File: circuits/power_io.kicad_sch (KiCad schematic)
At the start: 37 parts, among them J5 LASER PSU, J6 EXT 5V, U11 AP2112K-3.3, U12 INA4180A1, U13 LM4040C50 5V, U14 AD7606BSTZ-4

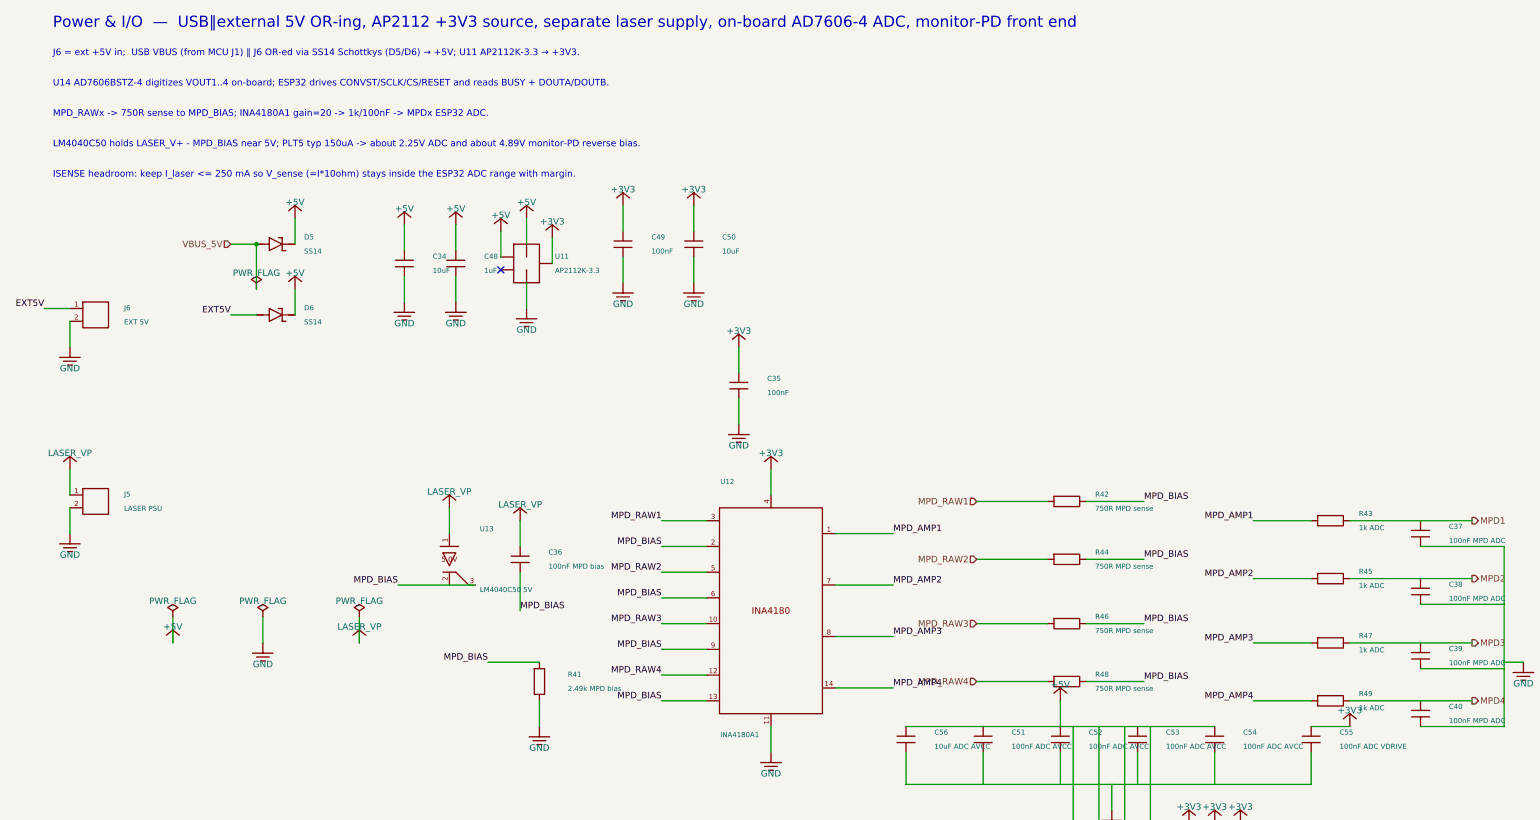
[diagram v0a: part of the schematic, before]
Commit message: add onboard laser controller supplies
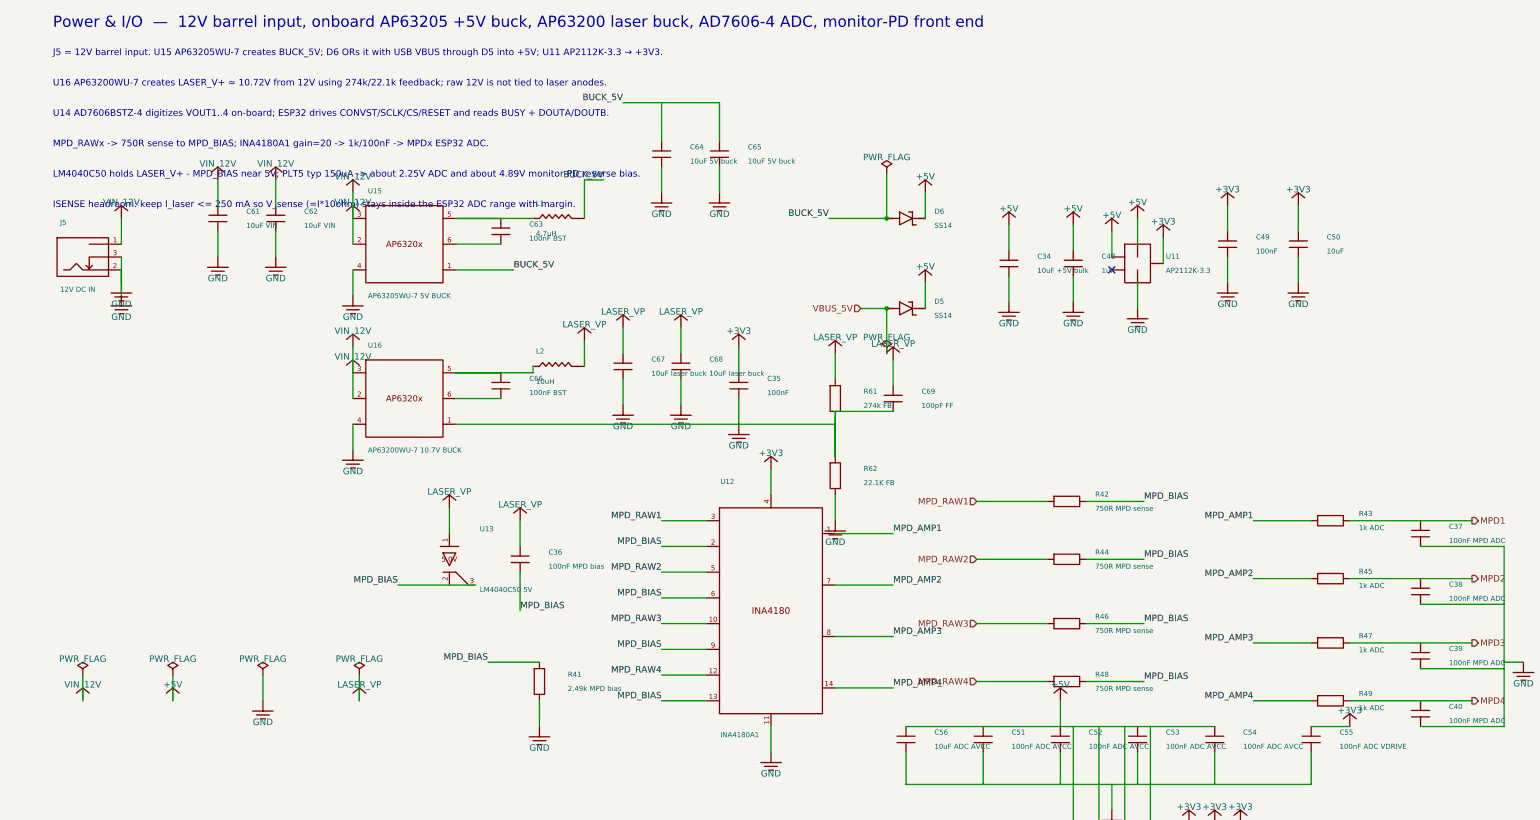
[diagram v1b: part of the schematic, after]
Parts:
- removed J5: LASER PSU, Connector_PinHeader_2.54mm:PinHeader_1x02_P2.54mm_Vertical, symbol viv:CONN2
- removed J6: EXT 5V, Connector_PinHeader_2.54mm:PinHeader_1x02_P2.54mm_Vertical, symbol viv:CONN2
- added C61, C62: 10uF VIN, Capacitor_SMD:C_0805_2012Metric_Pad1.18x1.45mm_HandSolder, symbol viv:C_V
- added C63, C66: 100nF BST, Capacitor_SMD:C_0402_1005Metric_Pad0.74x0.62mm_HandSolder, symbol viv:C_V
- added C64, C65: 10uF 5V buck, Capacitor_SMD:C_0805_2012Metric_Pad1.18x1.45mm_HandSolder, symbol viv:C_V
- added C67, C68: 10uF laser buck, Capacitor_SMD:C_0805_2012Metric_Pad1.18x1.45mm_HandSolder, symbol viv:C_V
- added C69: 100pF FF, Capacitor_SMD:C_0402_1005Metric_Pad0.74x0.62mm_HandSolder, symbol viv:C_V
- added D5: SS14, Diode_SMD:D_SMA, symbol viv:SCHOTTKY
- added L1: 4.7uH, Open_Automation:L_5.4x5.3_H3, symbol viv:L_H
- added L2: 10uH, Open_Automation:L_4x4, symbol viv:L_H
- added R61: 274k FB, Resistor_SMD:R_0603_1608Metric_Pad0.98x0.95mm_HandSolder, symbol viv:R_V
- added R62: 22.1K FB, Resistor_SMD:R_0402_1005Metric_Pad0.72x0.64mm_HandSolder, symbol viv:R_V
- added U15: AP63205WU-7 5V BUCK, Package_TO_SOT_SMD:TSOT-23-6, symbol viv:AP6320X_TSOT6
- added U16: AP63200WU-7 10.7V BUCK, Package_TO_SOT_SMD:TSOT-23-6, symbol viv:AP6320X_TSOT6
- C34: value 10uF -> 10uF +5V bulk
- J5: renamed from D5; value SS14 -> 12V DC IN; footprint Diode_SMD:D_SMA -> Open_Automation:BarrelJack_OD5.5_ID2.5; symbol viv:SCHOTTKY -> viv:BARREL_JACK_SWITCH; LCSC C2480 -> C194407; Part Number SS14 -> DC-470-2.1GP
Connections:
- net +5V: now also D5.2 (K); no longer J5.2 (K)
- net GND: now also J5.2, J5.3, C61.2, C62.2, C64.2, C65.2, C67.2, C68.2, R62.2, U15.4 (GND), U16.4 (GND)
- net LASER_V+: now also C67.1, C68.1, C69.1, L2.2, R61.1
- net VBUS_5V: now also D5.1 (A); no longer J5.1 (A)
- net EXT5V renamed BUCK_5V
- net BUCK_5V: now also C64.1, C65.1, L1.2, U15.1 (FB)
- new net: C63.1, L1.1, U15.5 (SW)
- new net: C63.2, U15.6 (BST)
- new net: C69.2, R61.2, R62.1, U16.1 (FB)
- new net: C66.1, L2.1, U16.5 (SW)
- new net: C66.2, U16.6 (BST)
- new net VIN_12V: C61.1, C62.1, J5.1, U15.2 (EN), U15.3 (IN), U16.2 (EN), U16.3 (IN)
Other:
- note added: "J5 = 12V barrel input. U15 AP63205WU-7 creates BUCK_5V; D6 ORs it with USB VBUS through D5 into +5V; U11 AP2112K-3.3 → +3V3."
- note added: "Power & I/O — 12V barrel input, onboard AP63205 +5V buck, AP63200 laser buck, AD7606-4 ADC, monitor-PD front end"
- note added: "U16 AP63200WU-7 creates LASER_V+ ≈ 10.72V from 12V using 274k/22.1k feedback; raw 12V is not tied to laser anodes."
- note removed: "J6 = ext +5V in; USB VBUS (from MCU J1) ‖ J6 OR-ed via SS14 Schottkys (D5/D6) → +5V; U11 AP2112K-3.3 → +3V3."
- note removed: "Power & I/O — USB‖external 5V OR-ing, AP2112 +3V3 source, separate laser supply, on-board AD7606-4 ADC, monitor-PD front end"

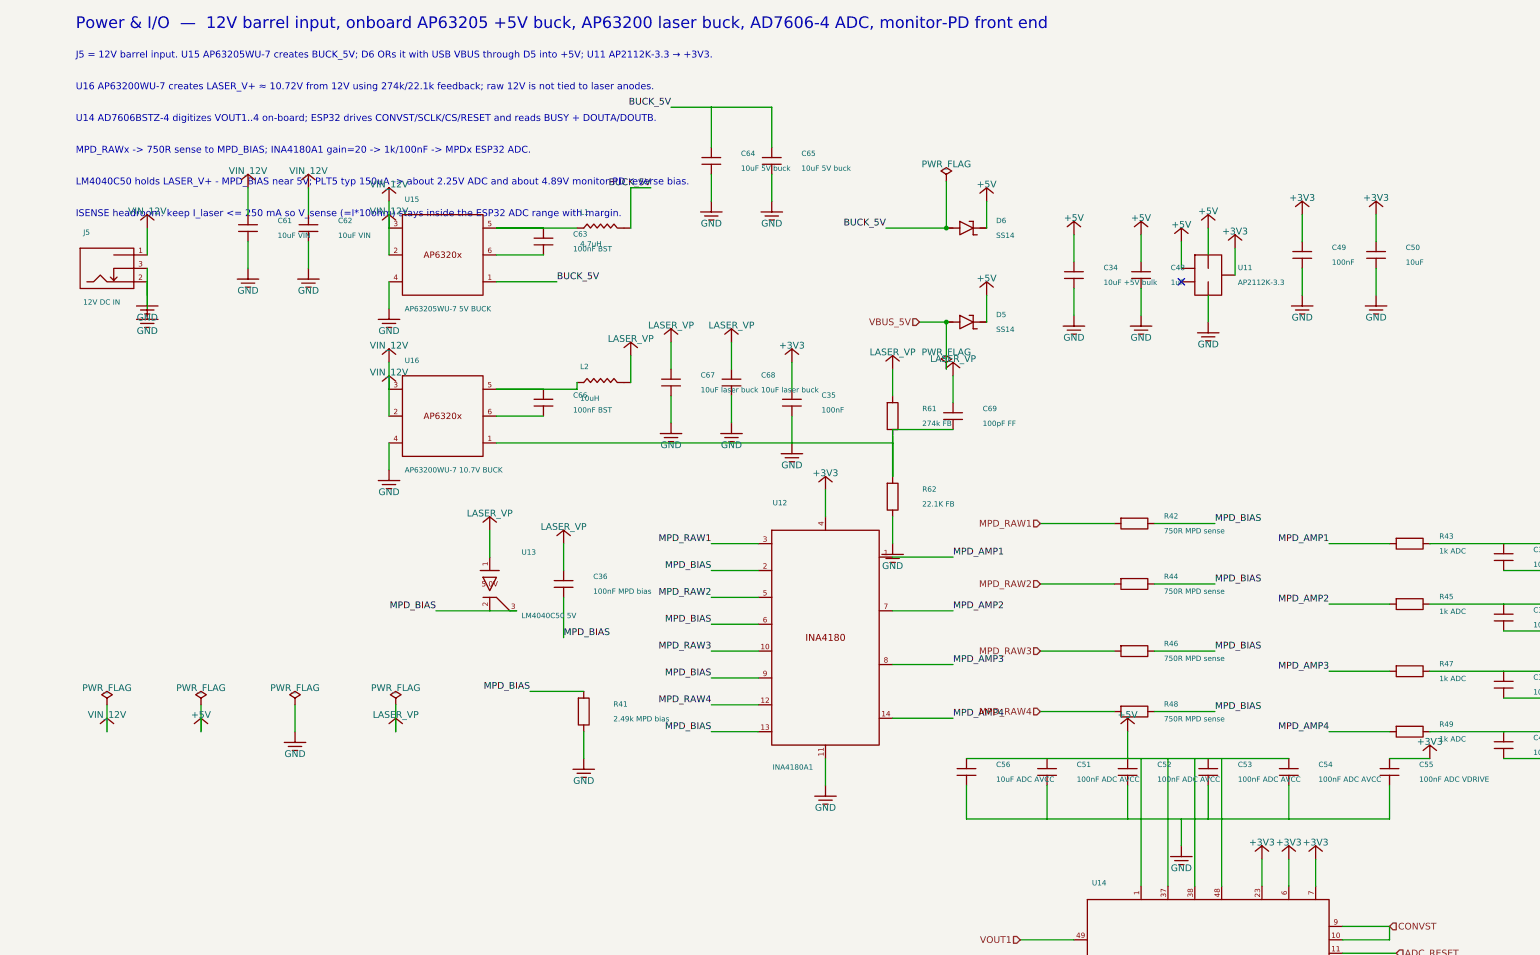
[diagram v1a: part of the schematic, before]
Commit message: Regenerate 24V power IO schematic
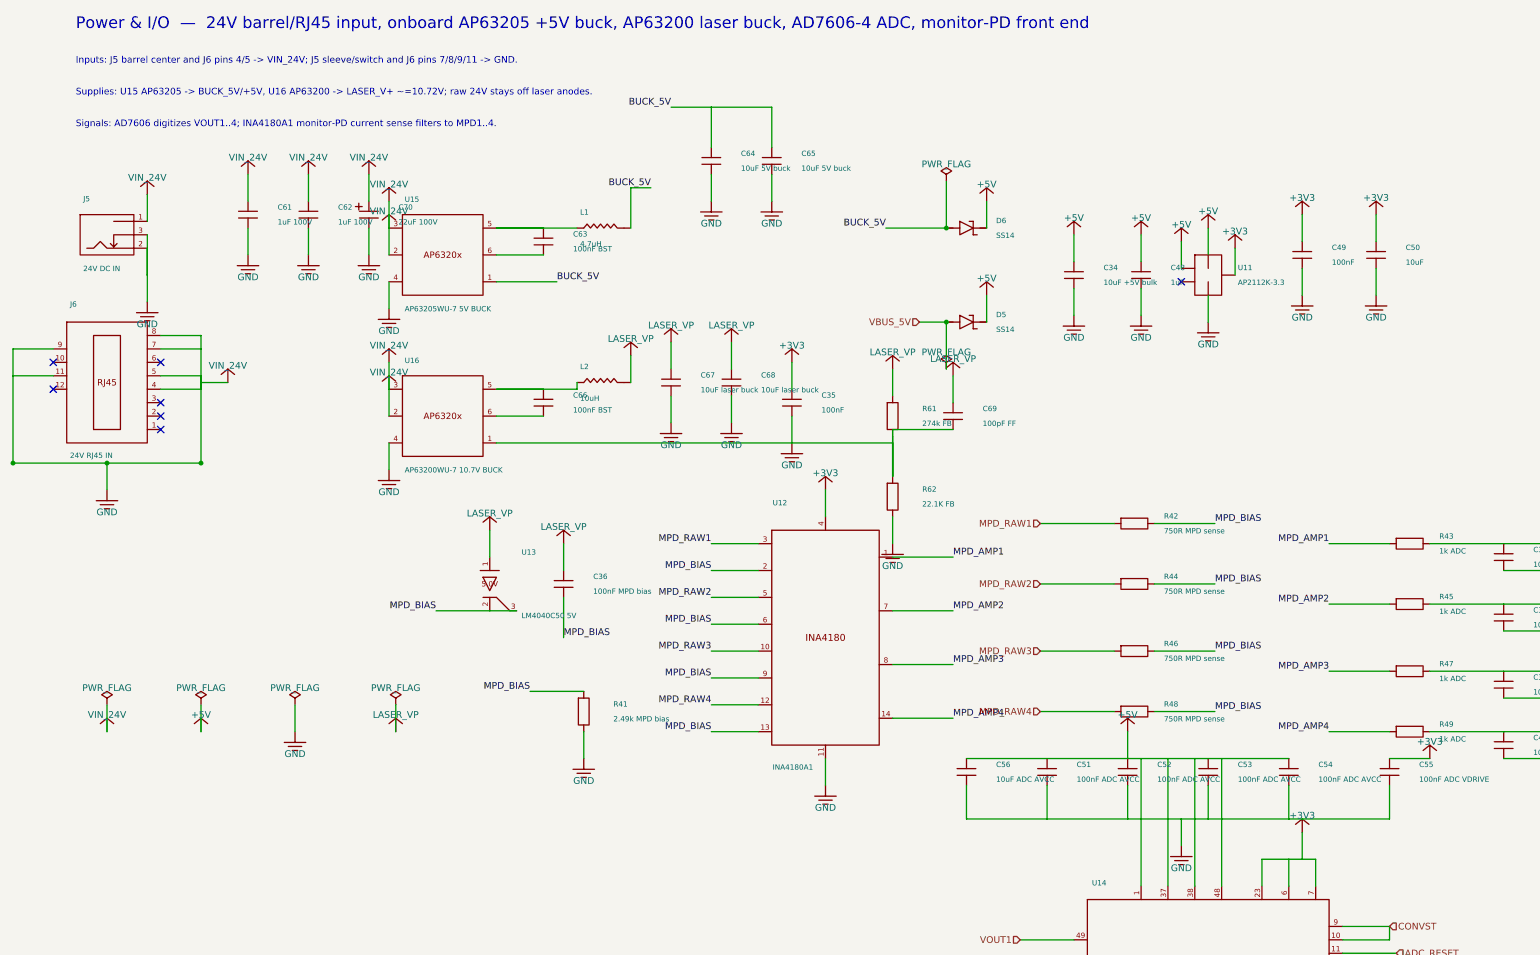
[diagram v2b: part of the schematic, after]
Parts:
- removed C48: 1uF, Capacitor_SMD:C_0402_1005Metric_Pad0.74x0.62mm_HandSolder, symbol viv:C_V
- removed C49: 100nF, Capacitor_SMD:C_0402_1005Metric_Pad0.74x0.62mm_HandSolder, symbol viv:C_V
- removed C50: 10uF, Capacitor_SMD:C_0805_2012Metric_Pad1.18x1.45mm_HandSolder, symbol viv:C_V
- removed C62: 10uF VIN, Capacitor_SMD:C_0805_2012Metric_Pad1.18x1.45mm_HandSolder, symbol viv:C_V
- removed U13: LM4040C50 5V, Package_TO_SOT_SMD:SOT-23, symbol viv:LM4040_DBZ
- removed U15: AP63205WU-7 5V BUCK, Package_TO_SOT_SMD:TSOT-23-6, symbol viv:AP6320X_TSOT6
- removed U16: AP63200WU-7 10.7V BUCK, Package_TO_SOT_SMD:TSOT-23-6, symbol viv:AP6320X_TSOT6
- added C63, C66: 100nF BST, Capacitor_SMD:C_0402_1005Metric_Pad0.74x0.62mm_HandSolder, symbol viv:C_V
- added C64, C65: 10uF 5V buck, Capacitor_SMD:C_0805_2012Metric_Pad1.18x1.45mm_HandSolder, symbol viv:C_V
- added C67, C68: 10uF laser buck, Capacitor_SMD:C_0805_2012Metric_Pad1.18x1.45mm_HandSolder, symbol viv:C_V
- added L1: 4.7uH, Open_Automation:L_5.4x5.3_H3, symbol viv:L_H
- added L2: 10uH, Open_Automation:L_4x4, symbol viv:L_H
- added R43: 1k ADC, Resistor_SMD:R_0603_1608Metric_Pad0.98x0.95mm_HandSolder, symbol viv:R_H
- C48: renamed from L2; value 10uH -> 1uF; footprint Open_Automation:L_4x4 -> Capacitor_SMD:C_0402_1005Metric_Pad0.74x0.62mm_HandSolder; symbol viv:L_H -> viv:C_V; LCSC C98364 -> C7472946; Part Number WPN4020H100MT -> HGC0402R5105K250NTEJ
- C49: renamed from C66; value 100nF BST -> 100nF
- C50: renamed from C67; value 10uF laser buck -> 10uF
- C61: renamed from L1; value 4.7uH -> 1uF 100V; footprint Open_Automation:L_5.4x5.3_H3 -> Capacitor_SMD:C_1206_3216Metric_Pad1.33x1.80mm_HandSolder; symbol viv:L_H -> viv:C_V; LCSC C408410 -> C13832; Part Number MWSA0503S-4R7MT -> CL31B105KCHNNNE
- C62: renamed from C63; value 100nF BST -> 1uF 100V; footprint Capacitor_SMD:C_0402_1005Metric_Pad0.74x0.62mm_HandSolder -> Capacitor_SMD:C_1206_3216Metric_Pad1.33x1.80mm_HandSolder; LCSC C83056 -> C13832; Part Number 0402B104K160CT -> CL31B105KCHNNNE
- C70: renamed from C64; value 10uF 5V buck -> 22uF 100V; footprint Capacitor_SMD:C_0805_2012Metric_Pad1.18x1.45mm_HandSolder -> Capacitor_SMD:C_Elec_8x10.2; symbol viv:C_V -> viv:C_POL_V; LCSC C318691 -> C90264; Part Number CL21A106KAYNNNG -> RVT2A220M0810
- J5: value 12V DC IN -> 24V DC IN
- J6: renamed from C61; value 10uF VIN -> 24V RJ45 IN; footprint Capacitor_SMD:C_0805_2012Metric_Pad1.18x1.45mm_HandSolder -> Connector_RJ:RJ45_Amphenol_RJHSE538X; symbol viv:C_V -> viv:CONN_RJ45; LCSC C318691 -> C386757; Part Number CL21A106KAYNNNG -> R-RJ45R08P-C000
- U13: renamed from R43; value 1k ADC -> LM4040C50 5V; footprint Resistor_SMD:R_0603_1608Metric_Pad0.98x0.95mm_HandSolder -> Package_TO_SOT_SMD:SOT-23; symbol viv:R_H -> viv:LM4040_DBZ; LCSC C2907002 -> C69316; Part Number FRC0603F1001TS -> LM4040C50IDBZR
- U15: renamed from C65; value 10uF 5V buck -> AP63205WU-7 5V BUCK; footprint Capacitor_SMD:C_0805_2012Metric_Pad1.18x1.45mm_HandSolder -> Package_TO_SOT_SMD:TSOT-23-6; symbol viv:C_V -> viv:AP6320X_TSOT6; LCSC C318691 -> C2071056; Part Number CL21A106KAYNNNG -> AP63205WU-7
- U16: renamed from C68; value 10uF laser buck -> AP63200WU-7 10.7V BUCK; footprint Capacitor_SMD:C_0805_2012Metric_Pad1.18x1.45mm_HandSolder -> Package_TO_SOT_SMD:TSOT-23-6; symbol viv:C_V -> viv:AP6320X_TSOT6; LCSC C318691 -> C2071868; Part Number CL21A106KAYNNNG -> AP63200WU-7
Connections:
- net +3V3: now also C49.1, C50.1
- net +5V: now also C48.1
- net BUCK_5V: now also C64.1, C65.1, L1.2; no longer C61.2, C70.1
- net GND: now also C48.2, C49.2, C61.1, C61.2, C62.1, C62.2, C70.1 (+), J5.1, J6.11, J6.4, J6.5, J6.7, J6.8, J6.9, U15.3 (IN), U15.4 (GND), U16.3 (IN), U16.4 (GND), C64.2, C65.2, C67.2, C68.2; no longer J6.2
- net LASER_V+: now also U13.1 (K), C67.1, C68.1, L2.2; no longer C48.2, C50.1, U16.1
- net MPD1: now also R43.2; no longer U13.2
- net MPD_AMP1: now also R43.1; no longer U13.1
- net MPD_BIAS: now also U13.2 (A), U13.3 (*)
- net at C69.2, R61.2, R62.1: now also U16.1 (FB)
- net VIN_12V: no longer names the net of J6.1
- net VIN_12V: no longer J5.1
- new net: C63.1, L1.1, U15.5 (SW)
- new net: C63.2, U15.6 (BST)
- new net: C66.1, L2.1, U16.5 (SW)
- new net: C66.2, U16.6 (BST)
- no-connect marks 2 -> 8
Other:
- note added: "Inputs: J5 barrel center and J6 pins 4/5 -> VIN_24V; J5 sleeve/switch and J6 pins 7/8/9/11 -> GND."
- note added: "Power & I/O — 24V barrel/RJ45 input, onboard AP63205 +5V buck, AP63200 laser buck, AD7606-4 ADC, monitor-PD front end"
- note added: "Signals: AD7606 digitizes VOUT1..4; INA4180A1 monitor-PD current sense filters to MPD1..4."
- note added: "Supplies: U15 AP63205 -> BUCK_5V/+5V, U16 AP63200 -> LASER_V+ ~=10.72V; raw 24V stays off laser anodes."
- note removed: "ISENSE headroom: keep I_laser <= 250 mA so V_sense (=I*10ohm) stays inside the ESP32 ADC range with margin."
- note removed: "J5 = 12V barrel input. U15 AP63205WU-7 creates BUCK_5V; D6 ORs it with USB VBUS through D5 into +5V; U11 AP2112K-3.3 → +3V3."
- note removed: "LM4040C50 holds LASER_V+ - MPD_BIAS near 5V; PLT5 typ 150uA -> about 2.25V ADC and about 4.89V monitor-PD reverse bias."
- note removed: "MPD_RAWx -> 750R sense to MPD_BIAS; INA4180A1 gain=20 -> 1k/100nF -> MPDx ESP32 ADC."
- note removed: "Power & I/O — 12V barrel input, onboard AP63205 +5V buck, AP63200 laser buck, AD7606-4 ADC, monitor-PD front end"
- note removed: "U14 AD7606BSTZ-4 digitizes VOUT1..4 on-board; ESP32 drives CONVST/SCLK/CS/RESET and reads BUSY + DOUTA/DOUTB."
- note removed: "U16 AP63200WU-7 creates LASER_V+ ≈ 10.72V from 12V using 274k/22.1k feedback; raw 12V is not tied to laser anodes."
- moved on the sheet: C49, C50, C62, J5
